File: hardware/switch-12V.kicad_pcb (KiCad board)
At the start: 2 copper layers, 48.3 x 54.6 mm, 27 parts, among them J1 CAN, J2 CAN, P1 CONN_PROG_AVR, P2 12V, P3 Pump, P4 Pump, P5 Pump, P6 Pump, Q1 photoMOS, Q2 photoMOS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

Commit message: Update footprint from module. Fix pad connection to ground plane.
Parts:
- C2, C3: value 22pF -> 33p
- moved R4 0.52 mm to (244.3, 118.6), turned to 180 degrees
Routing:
- net /12V-: track 50.7 -> 52.0 mm
- net Net-(R4-Pad2): track 2.36 -> 3.61 mm

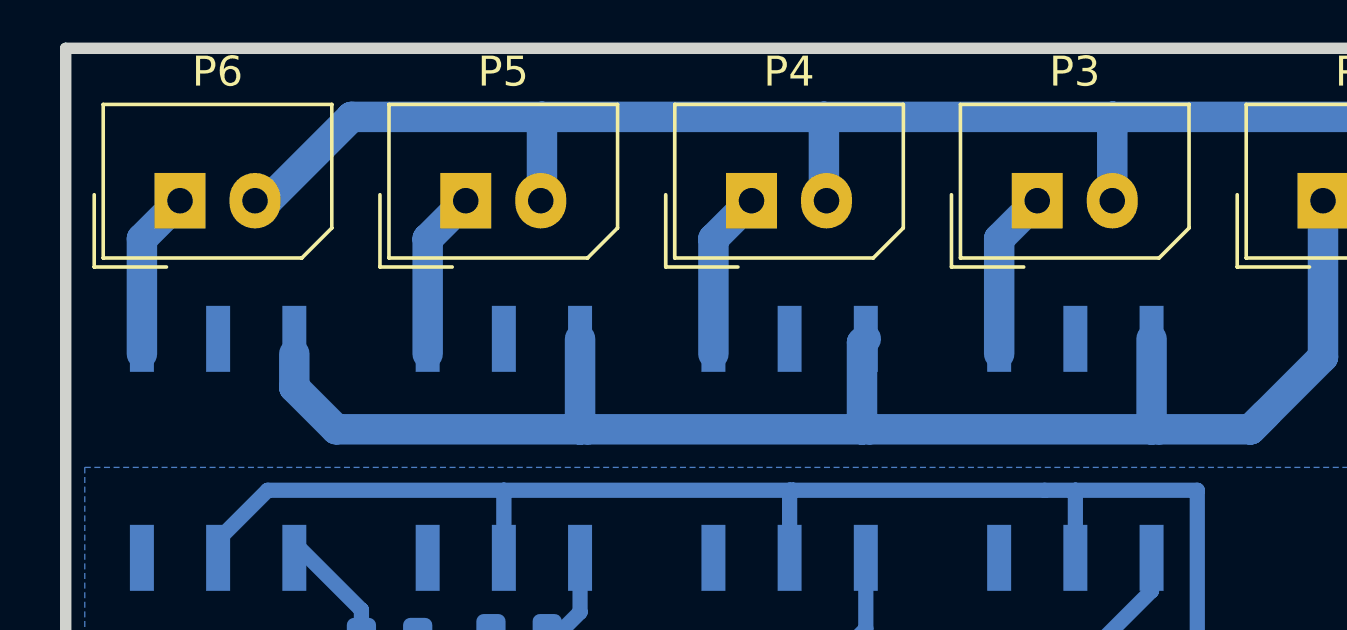
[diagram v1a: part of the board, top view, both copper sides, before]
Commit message: Fix relay wiring of 12V switch board
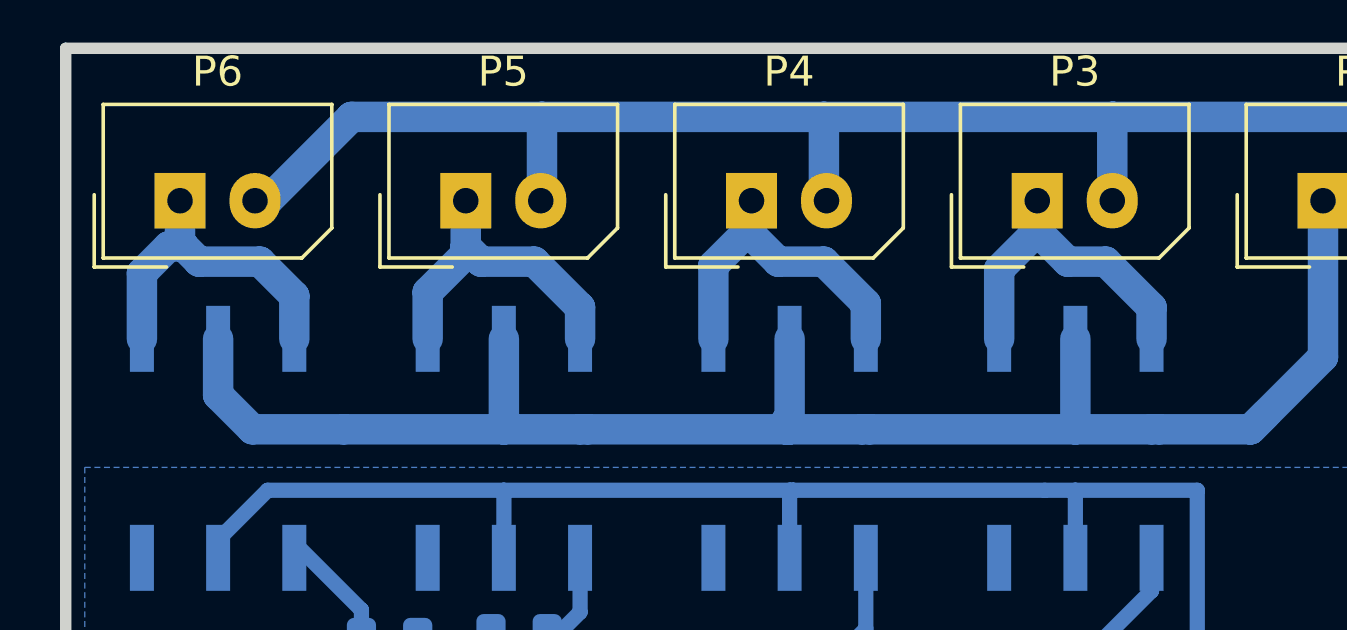
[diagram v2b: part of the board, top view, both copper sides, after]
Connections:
- Q1 pad 5: Net-(Q1-Pad5) -> /12V-
- Q1 pad 6: /12V- -> /X1
- Q2 pad 5: Net-(Q2-Pad5) -> /12V-
- Q2 pad 6: /12V- -> /X2
- Q3 pad 5: Net-(Q3-Pad5) -> /12V-
- Q3 pad 6: /12V- -> /X3
- Q4 pad 5: Net-(Q4-Pad5) -> /12V-
- Q4 pad 6: /12V- -> /X4
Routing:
- net /X4: track 5.63 -> 11.3 mm
- net /X2: track 5.63 -> 11.3 mm
- net /X1: track 5.63 -> 11.0 mm
- net /X3: track 5.63 -> 10.8 mm
- net /12V-: track 52.0 -> 56.2 mm
